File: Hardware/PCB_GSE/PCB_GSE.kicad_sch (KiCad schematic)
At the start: 32 parts, among them J4 Conn_01x06_Pin, U5 STM32F103CBT6, Y1 830050510

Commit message: feature : Done v1 and send to fab
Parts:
- C13, C18: DigiKey_Part_Number 1276-2891-1-ND -> 712-QSCT251Q220F1GV001ECT-ND; Manufacturer_Part_Number CL21A106KAYNNNE -> QSCT251Q220F1GV001E
- H1, H2, H3, H4, JP1: Manufacturer_Part_Number (none) -> -
- R13: DigiKey_Part_Number 311-10.0KHRCT-ND -> 311-10.0CRCT-ND; Manufacturer_Part_Number RC0603FR-0710KL -> RC0805FR-0710RL
- R17, R23, R24, R9: DigiKey_Part_Number 311-10.0KHRCT-ND -> 541-10.0KCCT-ND; Manufacturer_Part_Number RC0603FR-0710KL -> CRCW080510K0FKEA
- R6: DigiKey_Part_Number P1.5KDBCT-ND -> 311-1.50KCRCT-ND; Manufacturer_Part_Number ERA-3AEB152V -> RC0805FR-071K5L
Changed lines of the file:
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@@
 			)
 		)
-		(property "Datasheet" ""
+		(property "Datasheet" "-"
 			(at 139.7 186.69 0)
 			(effects
@@
 			)
 		)
+		(property "Manufacturer_Part_Number" "-"
+			(at 139.7 186.69 0)
+			(effects
+				(font
+					(size 1.27 1.27)
+				)
+				(hide yes)
+			)
+		)
 		(instances
 			(project "PCB_GSE"
@@
 			)
 		)
-		(property "Datasheet" "https://www.digikey.ca/en/products/detail/yageo/RC0603FR-0710KL/726880"
+		(property "Datasheet" "https://www.digikey.ca/en/products/detail/vishay-dale/CRCW080510K0FKEA/1175751"
 			(at 87.63 99.06 0)
 			(effects
@@
 			)
 		)
-		(property "DigiKey_Part_Number" "311-10.0KHRCT-ND"
+		(property "DigiKey_Part_Number" "541-10.0KCCT-ND"
 			(at 87.63 99.06 0)
 			(effects
@@
 			)
 		)
-		(property "Manufacturer_Part_Number" "RC0603FR-0710KL"
+		(property "Manufacturer_Part_Number" "CRCW080510K0FKEA"
 			(at 87.63 99.06 0)
 			(effects
@@
 			)
 		)
-		(property "Datasheet" "https://www.digikey.ca/en/products/detail/samsung-electro-mechanics/CL21A106KAYNNNE/3888549"
+		(property "Datasheet" "https://www.digikey.ca/en/products/detail/johanson-technology-inc/QSCT251Q220F1GV001E/1919484"
 			(at 242.57 101.6 0)
 			(effects
@@
 			)
 		)
-		(property "DigiKey_Part_Number" "1276-2891-1-ND"
+		(property "DigiKey_Part_Number" "712-QSCT251Q220F1GV001ECT-ND"
 			(at 242.57 101.6 0)
 			(effects
@@
 			)
 		)
-		(property "Manufacturer_Part_Number" "CL21A106KAYNNNE"
+		(property "Manufacturer_Part_Number" "QSCT251Q220F1GV001E"
 			(at 242.57 101.6 0)
 			(effects
@@
 			)
 		)
-		(property "Datasheet" "https://www.digikey.ca/en/products/detail/yageo/RC0603FR-0710KL/726880"
+		(property "Datasheet" "https://www.digikey.ca/en/products/detail/yageo/RC0805FR-0710RL/727534"
 			(at 266.7 91.44 0)
 			(effects
@@
 			)
 		)
-		(property "DigiKey_Part_Number" "311-10.0KHRCT-ND"
+		(property "DigiKey_Part_Number" "311-10.0CRCT-ND"
 			(at 266.7 91.44 0)
 			(effects
@@
 			)
 		)
-		(property "Manufacturer_Part_Number" "RC0603FR-0710KL"
+		(property "Manufacturer_Part_Number" "RC0805FR-0710RL"
 			(at 266.7 91.44 0)
 			(effects
@@
 			)
 		)
-		(property "Datasheet" "https://www.digikey.ca/en/products/detail/panasonic-electronic-components/ERA-3AEB152V/1465858"
+		(property "Datasheet" "https://www.digikey.ca/en/products/detail/yageo/RC0805FR-071K5L/727496"
 			(at 212.09 25.4 0)
 			(effects
@@
 			)
 		)
-		(property "DigiKey_Part_Number" "P1.5KDBCT-ND"
+		(property "DigiKey_Part_Number" "311-1.50KCRCT-ND"
 			(at 212.09 25.4 90)
 			(effects
@@
 			)
 		)
-		(property "Manufacturer_Part_Number" "ERA-3AEB152V"
+		(property "Manufacturer_Part_Number" "RC0805FR-071K5L"
 			(at 212.09 25.4 90)
 			(effects
@@
 			)
 		)
-		(property "Datasheet" ""
+		(property "Datasheet" "-"
 			(at 158.75 186.69 0)
 			(effects
@@
 			)
 		)
+		(property "Manufacturer_Part_Number" "-"
+			(at 158.75 186.69 0)
+			(effects
+				(font
+					(size 1.27 1.27)
+				)
+				(hide yes)
+			)
+		)
 		(instances
 			(project "PCB_GSE"
@@
 			)
 		)
-		(property "Datasheet" ""
+		(property "Datasheet" "-"
 			(at 158.75 191.77 0)
 			(effects
@@
 			)
 		)
+		(property "Manufacturer_Part_Number" "-"
+			(at 158.75 191.77 0)
+			(effects
+				(font
+					(size 1.27 1.27)
+				)
+				(hide yes)
+			)
+		)
 		(instances
 			(project "PCB_GSE"
@@
 			)
 		)
-		(property "Datasheet" ""
+		(property "Datasheet" "-"
 			(at 201.93 25.4 0)
 			(effects
@@
 			)
 		)
+		(property "Manufacturer_Part_Number" "-"
+			(at 201.93 25.4 0)
+			(effects
+				(font
+					(size 1.27 1.27)
+				)
+				(hide yes)
+			)
+		)
 		(pin "1"
 		)
@@
 			)
 		)
-		(property "Datasheet" "https://www.digikey.ca/en/products/detail/yageo/RC0603FR-0710KL/726880"
+		(property "Datasheet" "https://www.digikey.ca/en/products/detail/vishay-dale/CRCW080510K0FKEA/1175751"
 			(at 109.22 46.99 0)
 			(effects
@@
 			)
 		)
-		(property "DigiKey_Part_Number" "311-10.0KHRCT-ND"
+		(property "DigiKey_Part_Number" "541-10.0KCCT-ND"
 			(at 109.22 46.99 0)
 			(effects
@@
 			)
 		)
-		(property "Manufacturer_Part_Number" "RC0603FR-0710KL"
+		(property "Manufacturer_Part_Number" "CRCW080510K0FKEA"
 			(at 109.22 46.99 0)
 			(effects
@@
 			)
 		)
-		(property "Datasheet" ""
+		(property "Datasheet" "-"
 			(at 139.7 191.77 0)
 			(effects
@@
 			)
 		)
+		(property "Manufacturer_Part_Number" "-"
+			(at 139.7 191.77 0)
+			(effects
+				(font
+					(size 1.27 1.27)
+				)
+				(hide yes)
+			)
+		)
 		(instances
 			(project "PCB_GSE"
@@
 			)
 		)
-		(property "Datasheet" "https://www.digikey.ca/en/products/detail/yageo/RC0603FR-0710KL/726880"
+		(property "Datasheet" "https://www.digikey.ca/en/products/detail/vishay-dale/CRCW080510K0FKEA/1175751"
 			(at 95.25 99.06 0)
 			(effects
@@
 			)
 		)
-		(property "DigiKey_Part_Number" "311-10.0KHRCT-ND"
+		(property "DigiKey_Part_Number" "541-10.0KCCT-ND"
 			(at 95.25 99.06 0)
 			(effects
@@
 			)
 		)
-		(property "Manufacturer_Part_Number" "RC0603FR-0710KL"
+		(property "Manufacturer_Part_Number" "CRCW080510K0FKEA"
 			(at 95.25 99.06 0)
 			(effects
@@
 			)
 		)
-		(property "Datasheet" "https://www.digikey.ca/en/products/detail/samsung-electro-mechanics/CL21A106KAYNNNE/3888549"
+		(property "Datasheet" "https://www.digikey.ca/en/products/detail/johanson-technology-inc/QSCT251Q220F1GV001E/1919484"
 			(at 266.7 101.6 0)
 			(effects
@@
 			)
 		)
-		(property "DigiKey_Part_Number" "1276-2891-1-ND"
+		(property "DigiKey_Part_Number" "712-QSCT251Q220F1GV001ECT-ND"
 			(at 266.7 101.6 0)
 			(effects
@@
 			)
 		)
-		(property "Manufacturer_Part_Number" "CL21A106KAYNNNE"
+		(property "Manufacturer_Part_Number" "QSCT251Q220F1GV001E"
 			(at 266.7 101.6 0)
 			(effects
@@
 			)
 		)
-		(property "Datasheet" "https://www.digikey.ca/en/products/detail/yageo/RC0603FR-0710KL/726880"
+		(property "Datasheet" "https://www.digikey.ca/en/products/detail/vishay-dale/CRCW080510K0FKEA/1175751"
 			(at 218.44 30.48 0)
 			(effects
@@
 			)
 		)
-		(property "DigiKey_Part_Number" "311-10.0KHRCT-ND"
+		(property "DigiKey_Part_Number" "541-10.0KCCT-ND"
 			(at 218.44 30.48 0)
 			(effects
@@
 			)
 		)
-		(property "Manufacturer_Part_Number" "RC0603FR-0710KL"
+		(property "Manufacturer_Part_Number" "CRCW080510K0FKEA"
 			(at 218.44 30.48 0)
 			(effects

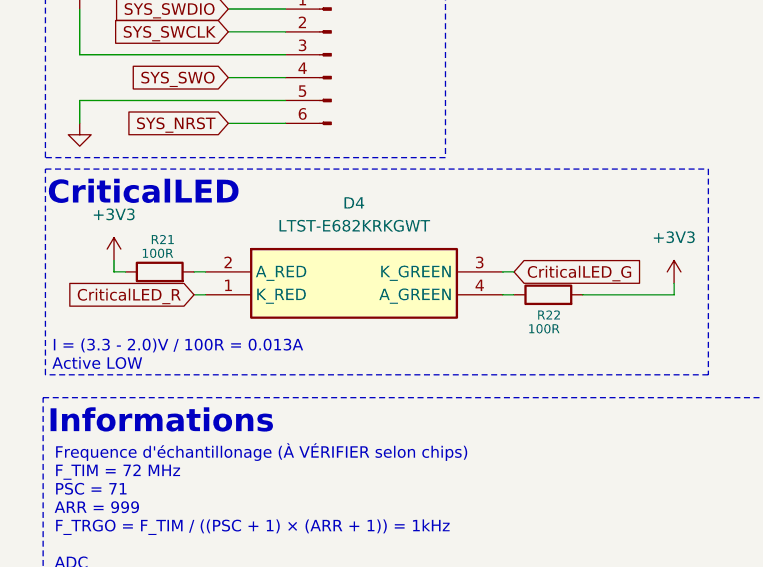
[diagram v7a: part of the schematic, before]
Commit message: fix(gse): change Swahelok S model -> Swagelok A model (adaptable) + 100R -> 100R 1% + silkscreen
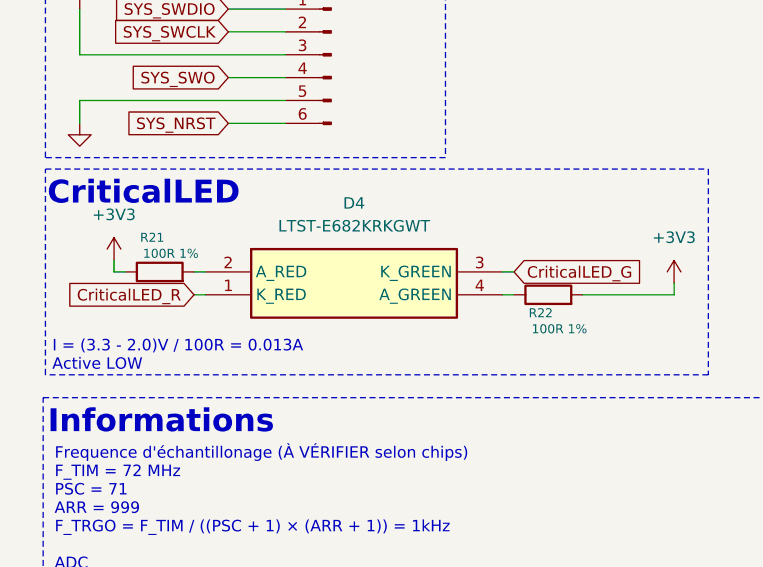
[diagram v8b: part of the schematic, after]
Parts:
- R21, R22: value 100R -> 100R 1%; DigiKey_Part_Number 541-100CCT-ND -> RT0805FRE07100RL; Manufacturer_Part_Number CRCW0805100RFKEA -> YAG3360CT-ND
